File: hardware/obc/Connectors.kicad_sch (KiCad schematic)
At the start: 17 parts, among them J13 USB_C_Receptacle_USB2.0, J16 1985807, J17 1985807, J18 1985807, J2 Conn_01x05, J3 1985807, J4 1985807, U7 Mem_MT29F4G01ABAFDWB, U8 Mem_MT29F4G01ABAFDWB

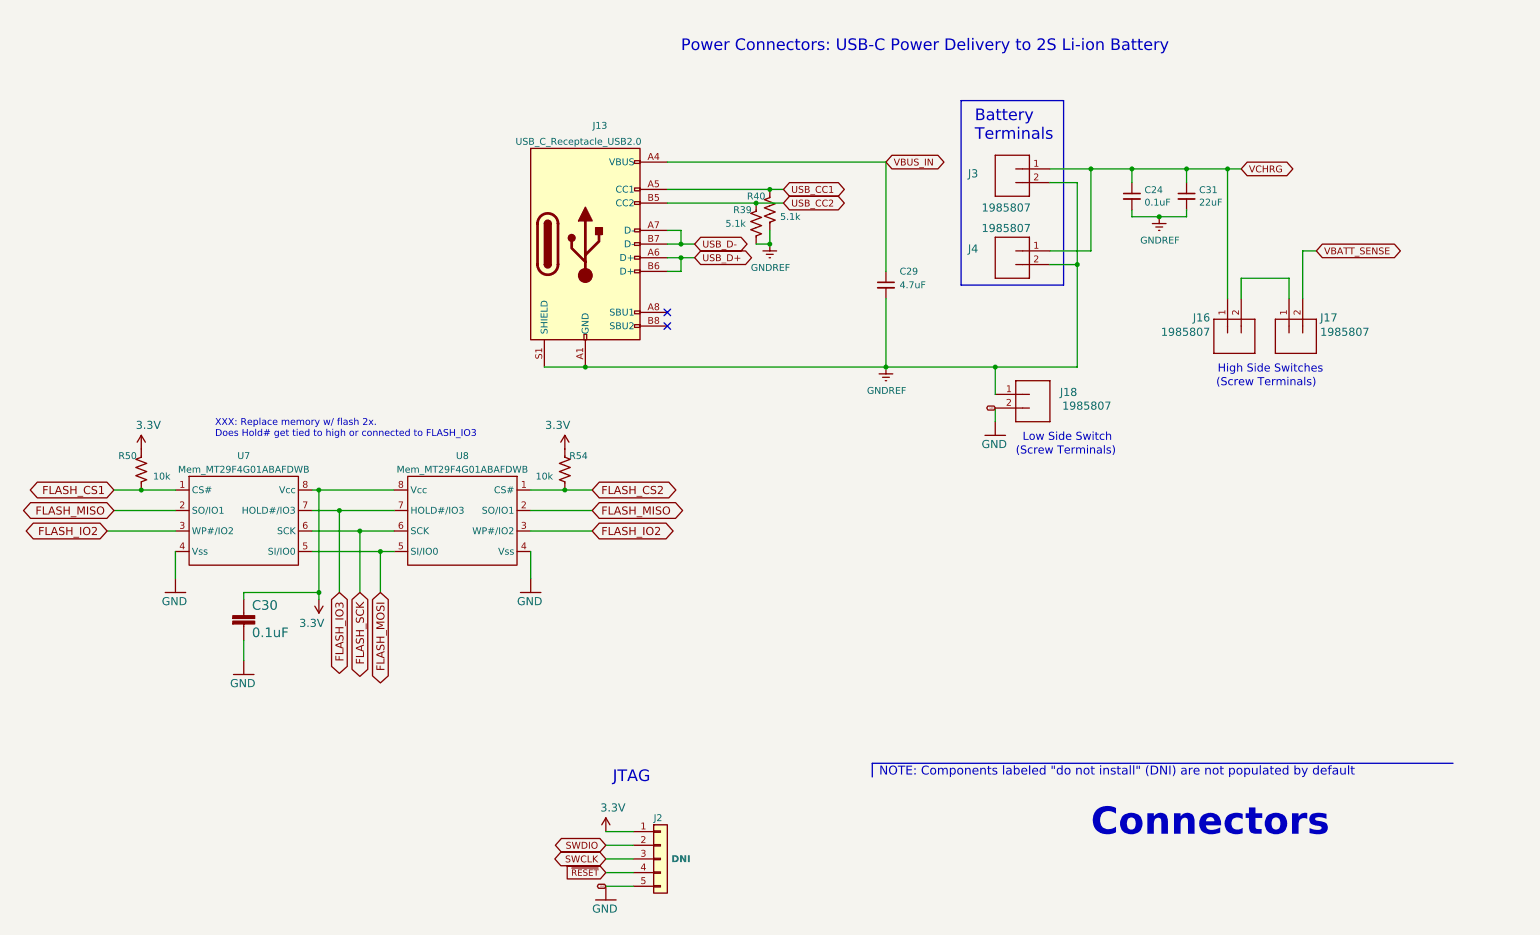
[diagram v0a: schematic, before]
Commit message: obc: Schematic pages to US Letter (except Power)
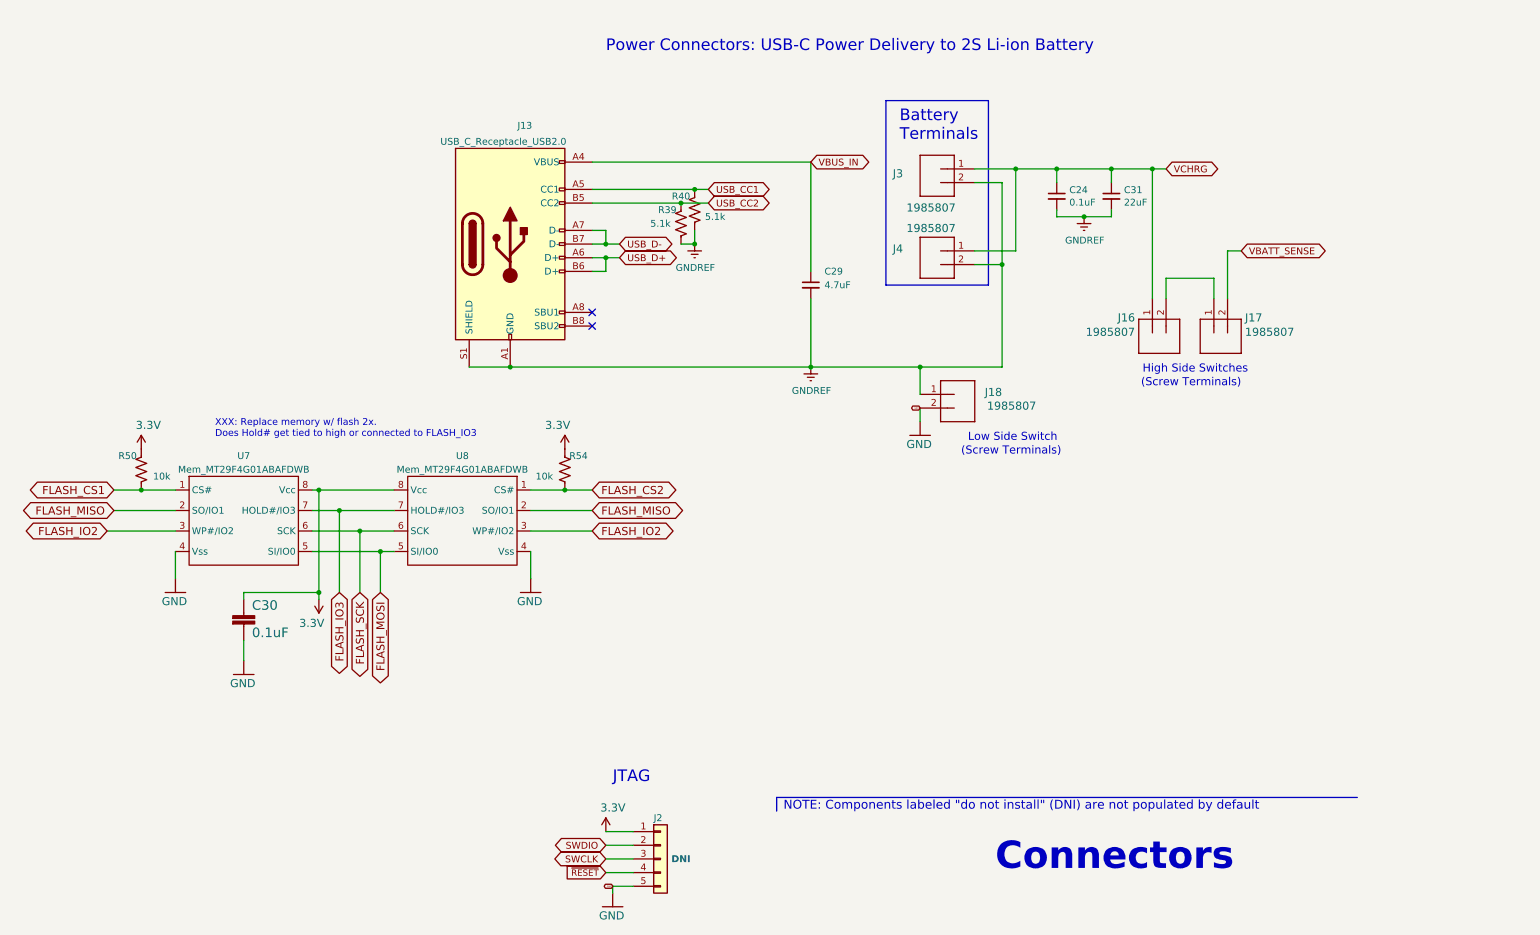
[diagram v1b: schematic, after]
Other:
- moved on the sheet: C24, C29, C31, J13, J16, J17, J18, J3, J4, R39, R40

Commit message: obc: Add many XXX comments documenting 5/3 review
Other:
- note added: "XXX - make into a single 6 pin hi-rel connector for interlock wire harness"
- note added: "XXX make into a single 2 high-power high-rel connector XXX put on the same connector (on finer pins) 3 more "grounds" (GNDREF) and 1 thermistor (ADC)"
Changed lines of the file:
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@@
+		)
+	)
+	(text "XXX - make into a single 6 pin hi-rel connector\nfor interlock wire harness"
+		(exclude_from_sim no)
+		(at 232.156 99.06 0)
+		(effects
+			(font
+				(size 1.27 1.27)
+			)
 		)
 	)
@@
 		)
 	)
+	(text "XXX make into a single 2 high-power high-rel connector\nXXX put on the same connector (on finer pins) 3 more \"grounds\" (GNDREF) and 1 thermistor (ADC)"
+		(exclude_from_sim no)
+		(at 189.738 35.306 0)
+		(effects
+			(font
+				(size 1.27 1.27)
+			)
+		)
+	)
 	(text "Power Connectors: USB-C Power Delivery to 2S Li-ion Battery"
 		(exclude_from_sim no)
-		(at 127 30.48 0)
+		(at 61.976 26.416 0)
 		(effects
 			(font

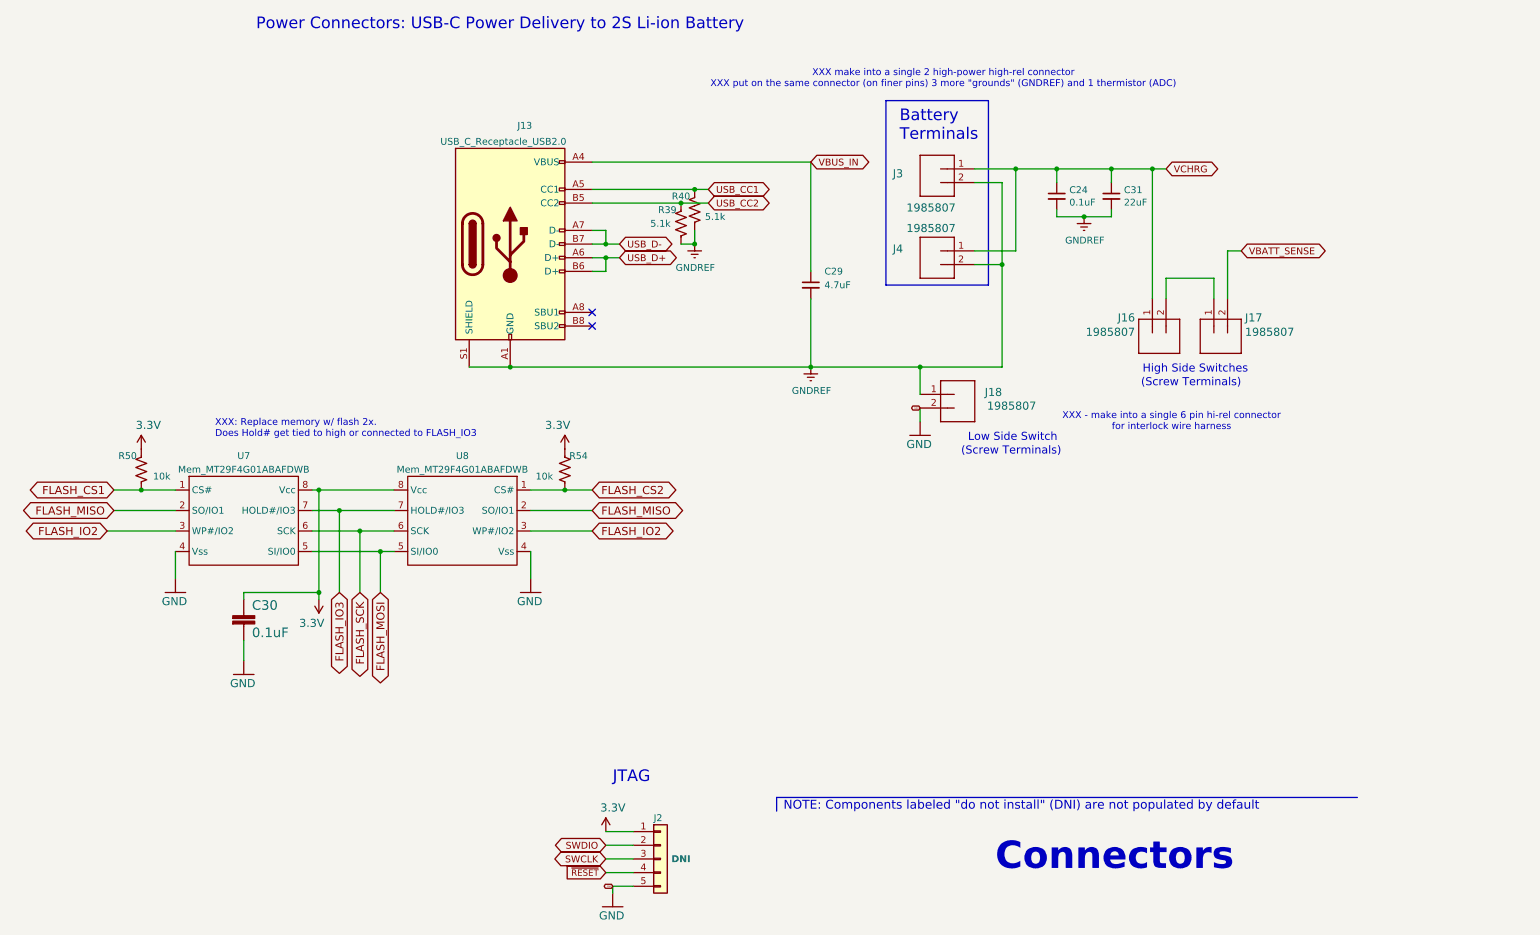
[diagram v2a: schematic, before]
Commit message: obc: schematic cleanup and wiring
Demarcated NC pins, added High-Rel connectors, cleaned up schematic legibility, and added bus protection for stacking signals SDA & SCL.
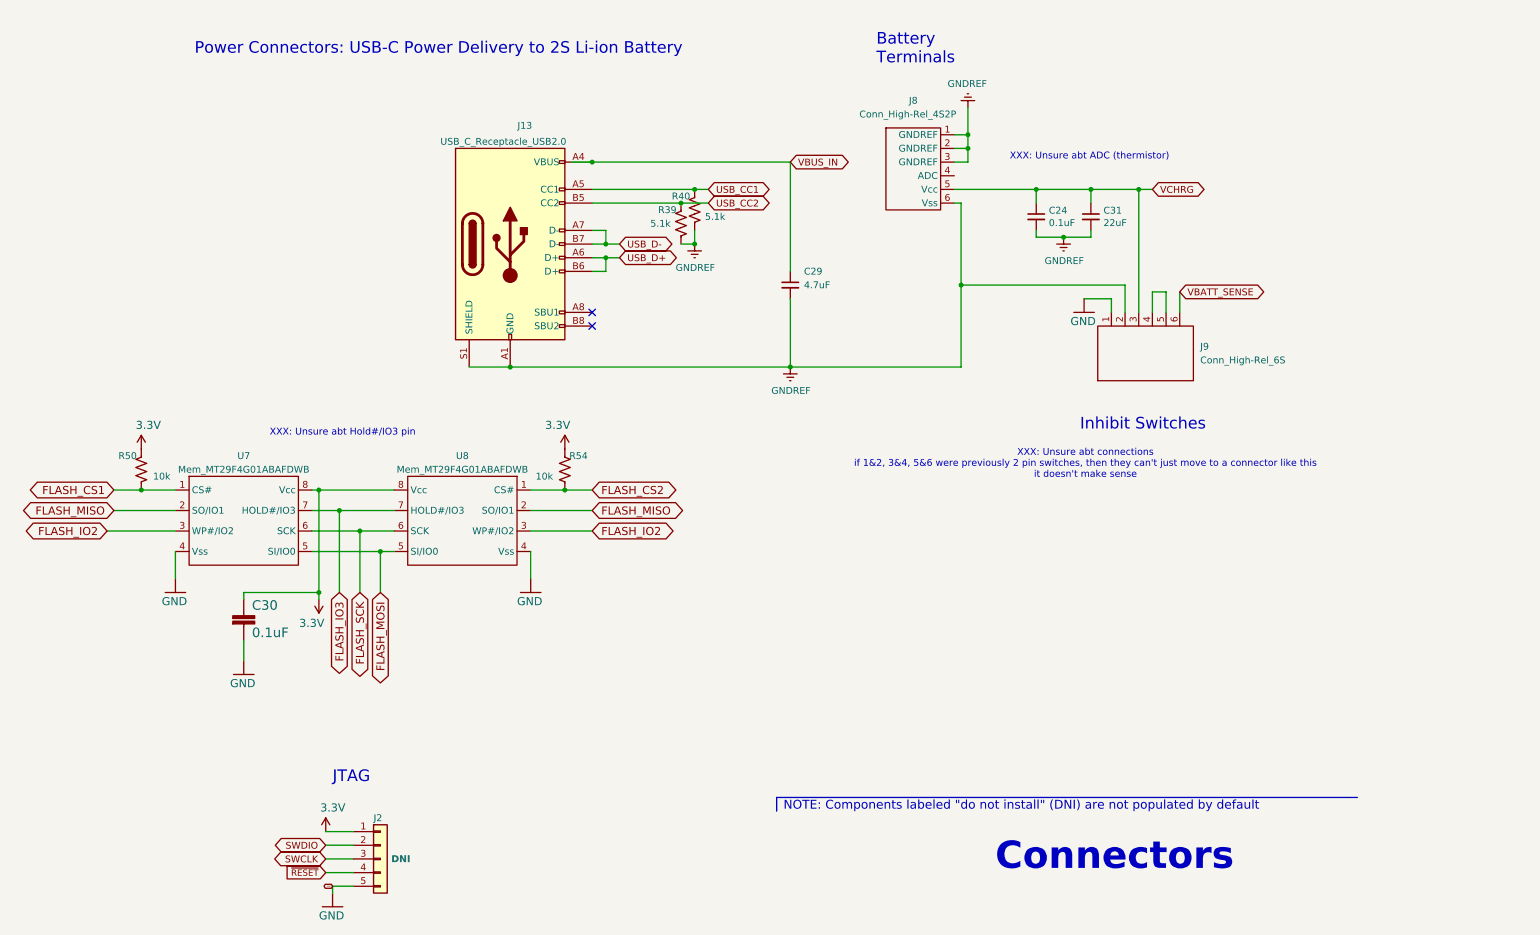
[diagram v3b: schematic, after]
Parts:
- removed J16, J17, J18, J3, J4: 1985807, mainboard:SCREWTERMINAL-3.5MM-2_LOCK, symbol mainboard:M023.5MM_LOCK
- added J8: Conn_High-Rel_4S2P, symbol SSE_Symbols:Conn_High-Rel_4S2P
- added J9: Conn_High-Rel_6S, symbol SSE_Symbols:Conn_High-Rel_6S
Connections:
- net GND: now also J9.1
- net GNDREF: now also J8.1 (GNDREF), J8.2 (GNDREF), J8.3 (GNDREF), J8.6 (Vss), J9.2
- net VBATT_SENSE: now also J9.6
- net VCHRG: now also J8.5 (Vcc), J9.3
- new net: J9.4, J9.5
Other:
- note added: "Inhibit Switches"
- note added: "XXX: Unsure abt ADC (thermistor)"
- note added: "XXX: Unsure abt Hold#/IO3 pin"
- note added: "XXX: Unsure abt connections if 1&2, 3&4, 5&6 were previously 2 pin switches, then they can't just move to a connector like this it doesn't make sense"
- note removed: "(Screw Terminals)"
- note removed: "High Side Switches"
- note removed: "Low Side Switch"
- note removed: "XXX - make into a single 6 pin hi-rel connector for interlock wire harness"
- note removed: "XXX make into a single 2 high-power high-rel connector XXX put on the same connector (on finer pins) 3 more "grounds" (GNDREF) and 1 thermistor (ADC)"
- note removed: "XXX: Replace memory w/ flash 2x. Does Hold# get tied to high or connected to FLASH_IO3"
- moved on the sheet: C24, C29, C31, J2

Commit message: obc: schematic editing and footprint development
Deleted irrelevant SD-related circuits and pins. Created new & modified existing connector and inductor footprints. Added new components (Bat Charger, High-Rel Connector, etc.)
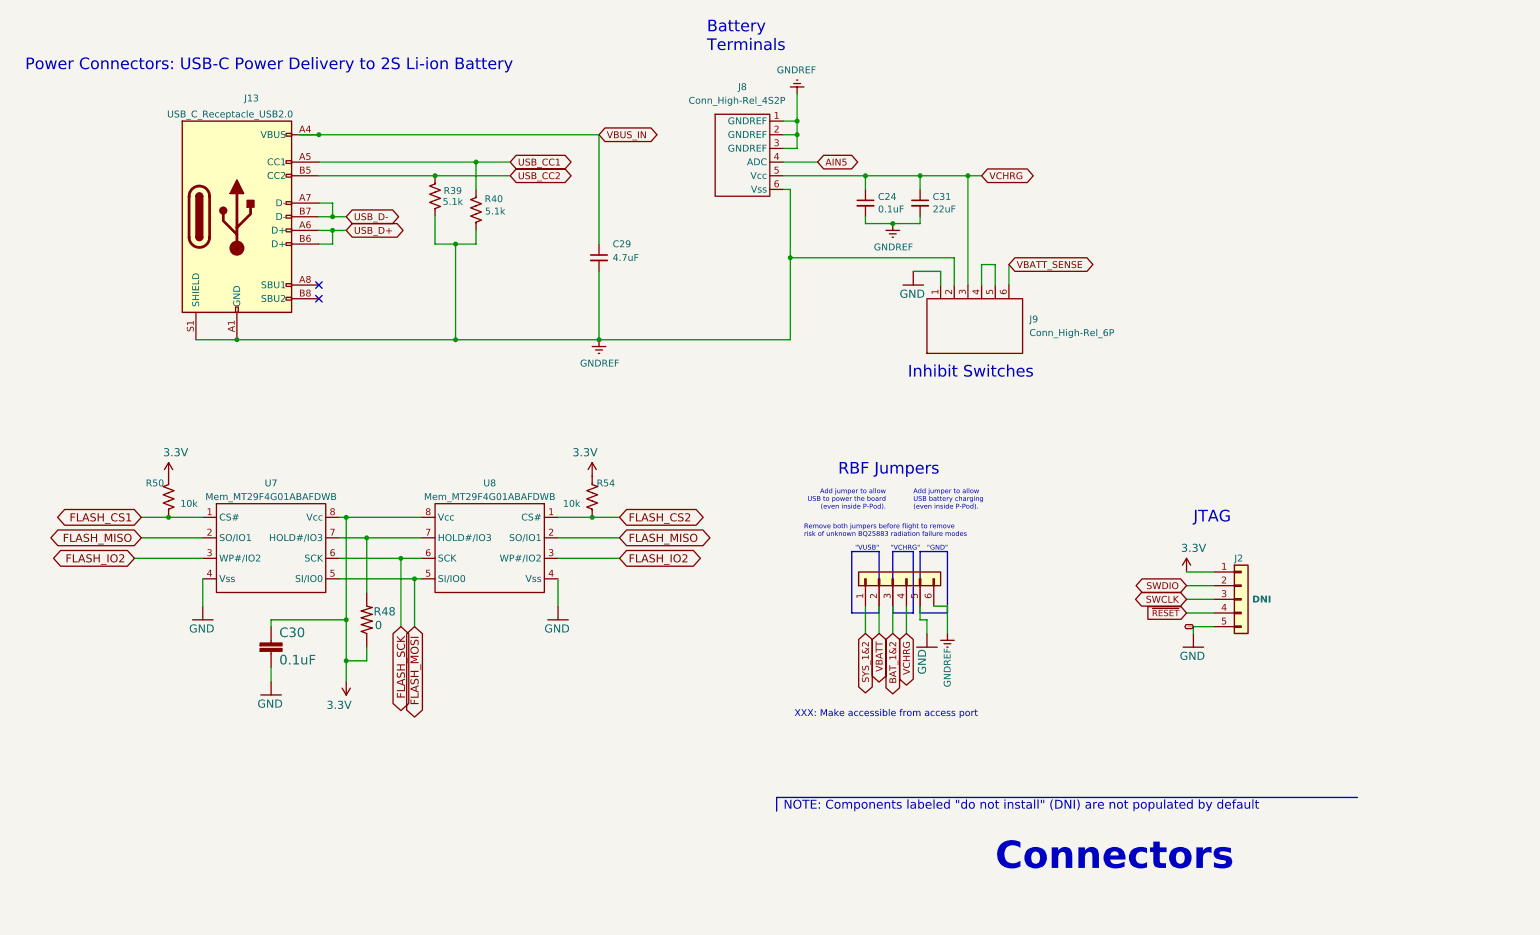
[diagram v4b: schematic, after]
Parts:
- added J3: Conn_01x06, Connector_PinHeader_2.54mm:PinHeader_1x06_P2.54mm_Vertical, symbol Connector_Generic:Conn_01x06
- added R48: 0, Resistor_SMD:R_0603_1608Metric, symbol mainboard:RESISTOR0603
- J8: Manufacturer_Part_Number (none) -> G125-MH104M3-02AD000P
- J9: value Conn_High-Rel_6S -> Conn_High-Rel_6P; Manufacturer_Part_Number (none) -> M300-MV30645M1
- U7, U8: footprint (none) -> SSE_Footprints:UPDFN-8_8.0x6.0mm_P1.27mm; LCSC (none) -> C2909506; Manufacturer_Name (none) -> Micron Technology; Manufacturer_Part_Number (none) -> MT29F4G01ABAFDWB-IT:F
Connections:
- net 3.3V: now also R48.1
- net GND: now also J3.5 (Pin_5)
- net GNDREF: now also J3.6 (Pin_6)
- net VCHRG: now also J3.4 (Pin_4)
- net AIN5: now reaches J8.4 (ADC)
- net FLASH_IO3: no longer names the net of U7.7 (HOLD#/IO3), U8.7 (HOLD#/IO3)
- net FLASH_IO3: now also R48.2
- new net BAT_1&2: J3.3 (Pin_3)
- new net SYS_1&2: J3.1 (Pin_1)
- new net VBATT: J3.2 (Pin_2)
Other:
- note added: ""GND""
- note added: ""VCHRG""
- note added: ""VUSB""
- note added: "Add jumper to allow USB battery charging (even inside P-Pod)."
- note added: "Add jumper to allow USB to power the board (even inside P-Pod)."
- note added: "RBF Jumpers"
- note added: "Remove both jumpers before flight to remove risk of unknown BQ25883 radiation failure modes"
- note added: "XXX: Make accessible from access port"
- note removed: "XXX: Unsure abt ADC (thermistor)"
- note removed: "XXX: Unsure abt Hold#/IO3 pin"
- note removed: "XXX: Unsure abt connections if 1&2, 3&4, 5&6 were previously 2 pin switches, then they can't just move to a connector like this it doesn't make sense"
- moved on the sheet: C24, C29, C30, C31, J13, J2, J8, J9, R39, R40, R50, R54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

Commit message: obc: BOM component verification
Verified part numbers, availability, values, footprints, etc. of components. Next steps involve verifying footprints and potentially researching some alternative components.
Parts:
- C29, C31: Notes (none) -> 10V ok?
- J13: footprint mainboard:USB_C_Receptacle_XKB_U262-161N-4BVC11 -> Connector_USB:USB_C_Receptacle_G-Switch_GT-USB-7010ASV; LCSC C319148 -> C2988369; Manufacturer_Name XKB Connectivity -> G-Switch; Manufacturer_Part_Number U262-161N-4BVC11 -> GT-USB-7010ASV
- J2: LCSC C2883762 -> (none); Notes (none) -> Not placed by JLCPCB
- J3: LCSC C2883763 -> (none); Notes (none) -> Not placed by JLCPCB
- J8: footprint (none) -> SSE_Footprints:Harwin_G125-MH104M3-02AD000P_4S2P_P1.25mm_Horizontal; Manufacturer_Name (none) -> Harwin
- J9: footprint (none) -> SSE_Footprints:Harwin_M300-MV30645M1_6P_P3.0mm_Vertical; Manufacturer_Name (none) -> Harwin
